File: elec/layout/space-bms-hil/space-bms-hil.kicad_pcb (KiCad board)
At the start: 4 copper layers, 90 x 70 mm, 135 parts, among them U1 10nF ±10% 50V X7R, U10 12.4kΩ ±1% 62.5mW, U100 1kΩ ±1% 62.5mW, U102 1kΩ ±1% 62.5mW, U105 10kΩ ±1% 62.5mW, U106 1kΩ ±1% 62.5mW, U108 1kΩ ±1% 62.5mW, U11 1nF ±10% 50V X7R, U12 220Ω ±1% 62.5mW, U13 1MΩ ±1% 62.5mW, U15 10pF ±5% 50V C0G, U16 10pF ±5% 50V C0G, U19 10nF ±10% 50V X7R, U2 220Ω ±1% 62.5mW, U20 6.8nF ±10% 50V X7R, U21 33Ω ±1% 62.5mW, U22 49.9Ω ±1% 62.5mW, U23 6.8nF ±10% 50V X7R, U24 33Ω ±1% 62.5mW, U25 49.9Ω ±1% 62.5mW, U26 4.7µF ±10% 10V X5R, U27 22nF ±10% 50V X7R, U28 10Ω ±1% 62.5mW, U29 33Ω ±1% 62.5mW, U3 10µF ±10% 25V X5R, U30 49.9Ω ±1% 62.5mW, U31 33Ω ±1% 62.5mW, U32 49.9Ω ±1% 62.5mW, U34 10µF ±10% 25V X5R, U35 10µF ±10% 25V X5R, U37 10kΩ ±1% 62.5mW, U39 10kΩ ±1% 62.5mW, U4 100nF ±10% 16V X7R, U41 100nF ±10% 16V X7R, U42 100nF ±10% 16V X7R, U43 2.2µF ±10% 25V X5R, U45 10kΩ ±1% 62.5mW, U46 10kΩ ±1% 62.5mW, U47 10kΩ ±1% 62.5mW, U48 10kΩ ±1% 62.5mW, U49 10kΩ ±1% 62.5mW, U5 100nF ±10% 16V X7R, U50 10kΩ ±1% 62.5mW, U51 10kΩ ±1% 62.5mW, U52 10kΩ ±1% 62.5mW, U53 10kΩ ±1% 62.5mW, U54 10kΩ ±1% 62.5mW, U55 10kΩ ±1% 62.5mW, U56 10kΩ ±1% 62.5mW, U57 10kΩ ±1% 62.5mW, U58 10kΩ ±1% 62.5mW, U59 10kΩ ±1% 62.5mW, U6 100nF ±10% 16V X7R, U60 10kΩ ±1% 62.5mW, U61 10kΩ ±1% 62.5mW, U62 10kΩ ±1% 62.5mW, U63 10kΩ ±1% 62.5mW, U66 100nF ±10% 16V X7R, U67 1kΩ ±1% 62.5mW, U68 10kΩ ±1% 62.5mW, U69 10kΩ ±1% 62.5mW, U7 100nF ±10% 16V X7R, U72 100nF ±10% 16V X7R, U73 1kΩ ±1% 62.5mW, U74 10kΩ ±1% 62.5mW, U75 10kΩ ±1% 62.5mW, U78 100nF ±10% 16V X7R, U79 1kΩ ±1% 62.5mW, U8 100nF ±10% 16V X7R, U80 10kΩ ±1% 62.5mW, U81 10kΩ ±1% 62.5mW, U84 100nF ±10% 16V X7R, U85 1kΩ ±1% 62.5mW, U86 1kΩ ±1% 62.5mW, U87 1kΩ ±1% 62.5mW, U88 1µF ±10% 25V X5R, U9 100nF ±10% 16V X7R, U90 1µF ±10% 25V X5R, U91 470nF ±20% 16V X5R, U92 1kΩ ±1% 62.5mW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

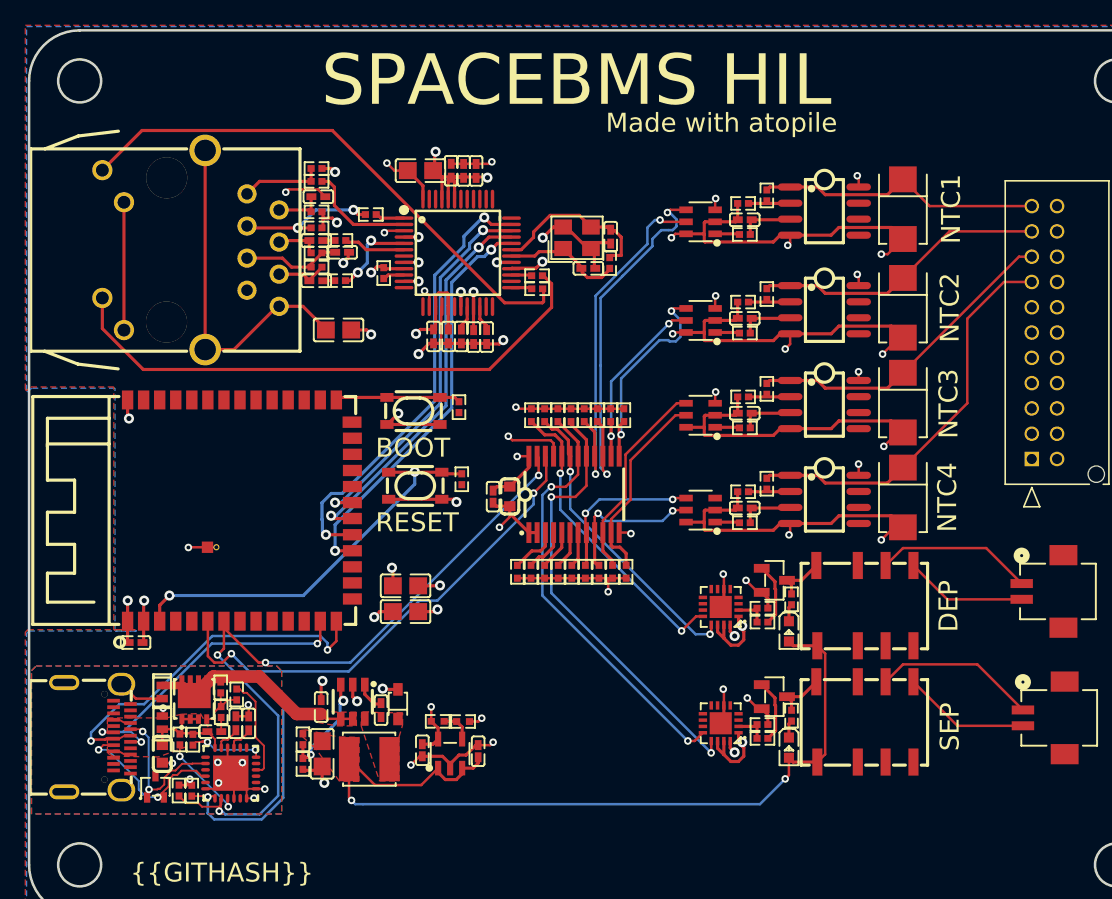
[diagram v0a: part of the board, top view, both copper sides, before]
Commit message: remove default build, build everything locally
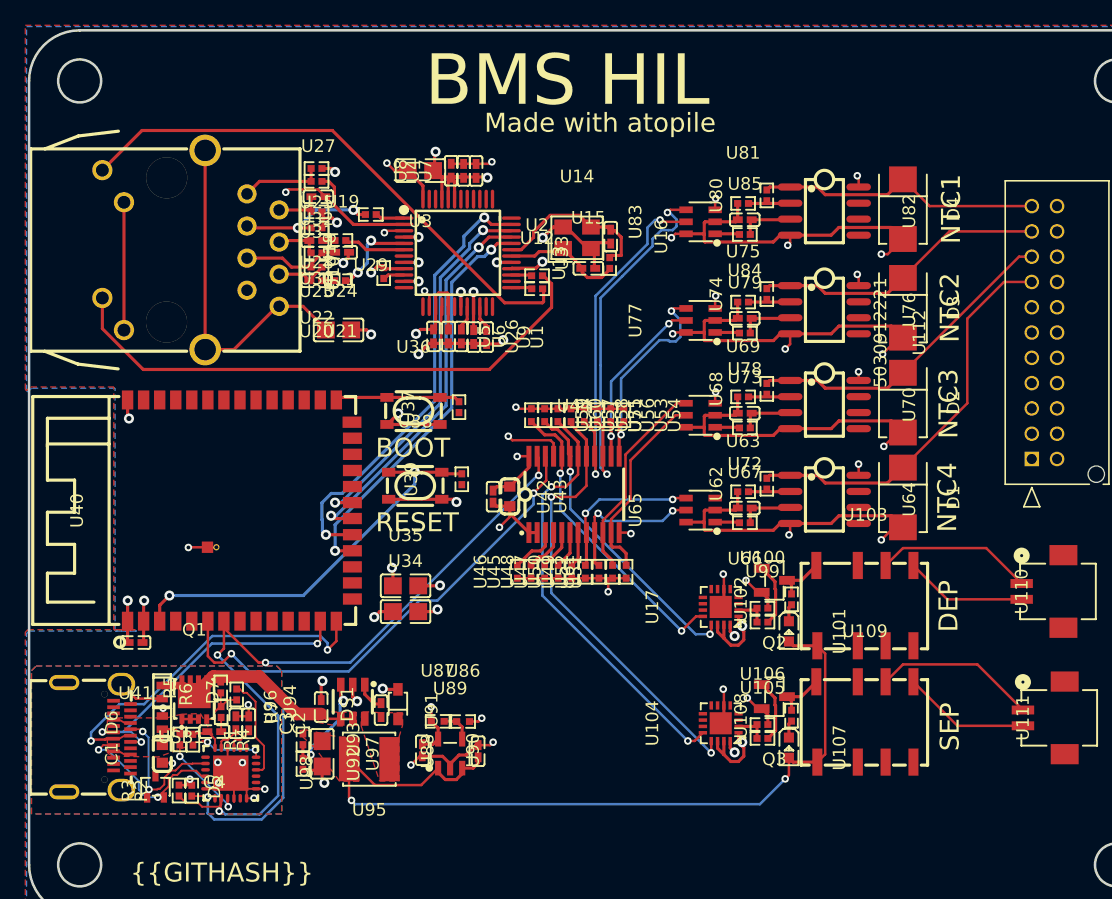
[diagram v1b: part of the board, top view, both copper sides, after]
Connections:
- net ADJ_NC renamed regulator_3v3-out
- net RESET_ renamed i2c_multiplexer-io
- net out renamed regulator_5v-out
- D1 pad 1: io-1 -> io-3
- D3 pad 1: io-2 -> io-1
- D4 pad 1: io-3 -> io-2
- DS1 pad 1: cathode-2 -> cathode-1
- R2 pad 1: line-10 -> line-9
- R3 pad 1: line-8 -> line-3
- U103 pad 5: hv-3 -> hv-1
- U104 pad 10: sep_relay.gpio_expander-net-4 -> sep_relay.gpio_expander-net-3
- U104 pad 12: line-2 -> line-10
- U104 pad 13: line-12 -> line-2
- U104 pad 3: sep_relay.gpio_expander-net-3 -> sep_relay.gpio_expander-net-1
- U104 pad 4: sep_relay.gpio_expander-net -> sep_relay.gpio_expander-net-5
- U104 pad 5: sep_relay.gpio_expander-net-5 -> sep_relay.gpio_expander-net-2
- U104 pad 7: sep_relay.gpio_expander-net-2 -> sep_relay.gpio_expander-net-4
- U104 pad 8: sep_relay.gpio_expander-net-6 -> sep_relay.gpio_expander-net
- U104 pad 9: sep_relay.gpio_expander-net-1 -> sep_relay.gpio_expander-net-6
- U107 pad 1: cathode-1 -> cathode-2
- U108 pad 1: cathode-1 -> cathode-2
- U109 pad 3: sep_relay-gnd-1 -> sep_relay-gnd
- U109 pad 4: sep_relay-gnd -> sep_relay-gnd-1
- U109 pad 6: hv-1 -> hv-3
- U110 pad 2: hv-3 -> hv-1
- U111 pad 1: hv-1 -> hv-3
- U112 pad 1: vsh_connector-net-7 -> vsh_connector-net-8
- U112 pad 10: vsh_connector-net -> vsh_connector-net-4
- U112 pad 11: vsh_connector-net-10 -> vsh_connector-net-9
- U112 pad 12: vsh_connector-net-9 -> vsh_connector-net-12
- U112 pad 13: vsh_connector-net-2 -> vsh_connector-net-10
- U112 pad 14: vsh_connector-net-1 -> vsh_connector-net
- U112 pad 15: io-1 -> io-3
- U112 pad 19: io-2 -> io-1
- U112 pad 2: vsh_connector-net-3 -> vsh_connector-net-1
- U112 pad 21: io-3 -> io-2
- U112 pad 3: vsh_connector-net-6 -> vsh_connector-net-13
- U112 pad 4: vsh_connector-net-8 -> vsh_connector-net-11
- U112 pad 5: vsh_connector-net-13 -> vsh_connector-net-6
- U112 pad 6: vsh_connector-net-11 -> vsh_connector-net-7
- U112 pad 7: vsh_connector-net-4 -> vsh_connector-net-2
- U112 pad 8: vsh_connector-net-12 -> vsh_connector-net-5
- U112 pad 9: vsh_connector-net-5 -> vsh_connector-net-3
- U17 pad 10: dep_relay.gpio_expander-net-3 -> dep_relay.gpio_expander-net-4
- U17 pad 12: line-3 -> line-5
- U17 pad 13: line-11 -> line-4
- U17 pad 3: dep_relay.gpio_expander-net-4 -> dep_relay.gpio_expander-net-1
- U17 pad 4: dep_relay.gpio_expander-net-5 -> dep_relay.gpio_expander-net-6
- U17 pad 5: dep_relay.gpio_expander-net-2 -> dep_relay.gpio_expander-net
- U17 pad 7: dep_relay.gpio_expander-net -> dep_relay.gpio_expander-net-2
- U17 pad 8: dep_relay.gpio_expander-net-6 -> dep_relay.gpio_expander-net-5
- U17 pad 9: dep_relay.gpio_expander-net-1 -> dep_relay.gpio_expander-net-3
- U40 pad 6: line-10 -> line-9
- U40 pad 7: line-8 -> line-3
- U44 pad 10: line-6 -> line-11
- U44 pad 11: line-5 -> line-7
- U44 pad 13: line-4 -> line-6
- U44 pad 14: line-9 -> line
- U44 pad 15: line-13 -> line-12
- U44 pad 16: line -> line-13
- U44 pad 17: line-12 -> line-2
- U44 pad 18: line-2 -> line-10
- U44 pad 19: line-11 -> line-4
- U44 pad 20: line-3 -> line-5
- U44 pad 22: line-10 -> line-9
- U44 pad 23: line-8 -> line-3
- U44 pad 4: i2c_multiplexer-line-3 -> i2c_multiplexer-line-2
- U44 pad 5: i2c_multiplexer-line-2 -> i2c_multiplexer-line-3
- U44 pad 9: line-7 -> line-8
- U45 pad 2: i2c_multiplexer-line-2 -> i2c_multiplexer-line-3
- U46 pad 2: i2c_multiplexer-line-3 -> i2c_multiplexer-line-2
- U49 pad 2: line-7 -> line-8
- U51 pad 2: line-5 -> line-7
- U52 pad 2: line-6 -> line-11
- U53 pad 2: line-9 -> line
- U54 pad 2: line-4 -> line-6
- U55 pad 2: line -> line-13
- U56 pad 2: line-13 -> line-12
- U57 pad 2: line-2 -> line-10
- U58 pad 2: line-12 -> line-2
- U59 pad 2: line-3 -> line-5
- U60 pad 2: line-11 -> line-4
- U62 pad 2: io-1 -> io-3
- U64 pad 1: io-1 -> io-3
- U64 pad 3: non_inverting-1 -> non_inverting
- U65 pad 5: line-7 -> line-8
- U66 pad 1: non_inverting-1 -> non_inverting
- U67 pad 2: non_inverting-1 -> non_inverting
- U70 pad 3: non_inverting -> non_inverting-1
- U71 pad 4: line-6 -> line-11
- U71 pad 5: line-5 -> line-7
- U72 pad 1: non_inverting -> non_inverting-1
- U73 pad 2: non_inverting -> non_inverting-1
- U74 pad 1: inverting -> inverting-3
- U74 pad 2: io-2 -> io-1
- U75 pad 2: inverting -> inverting-3
- U76 pad 1: io-2 -> io-1
- U76 pad 2: inverting -> inverting-3
- U76 pad 3: non_inverting-3 -> non_inverting-2
- U77 pad 4: line-4 -> line-6
- U77 pad 5: line-9 -> line
- U78 pad 1: non_inverting-3 -> non_inverting-2
- U79 pad 2: non_inverting-3 -> non_inverting-2
- U80 pad 1: inverting-3 -> inverting
- U80 pad 2: io-3 -> io-2
- U81 pad 2: inverting-3 -> inverting
- U82 pad 1: io-3 -> io-2
- U82 pad 2: inverting-3 -> inverting
- U82 pad 3: non_inverting-2 -> non_inverting-3
- U83 pad 4: line-13 -> line-12
- U83 pad 5: line -> line-13
- U84 pad 1: non_inverting-2 -> non_inverting-3
- U85 pad 2: non_inverting-2 -> non_inverting-3
- U91 pad 2: cathode-2 -> cathode-1
- U94 pad 6: cathode-2 -> cathode-1
- U95 pad 1: cathode-2 -> cathode-1
- U98 pad 1: usb_pd.pd_controller.pd_controller-line -> usb_pd.pd_controller.pd_controller-line-1
- U98 pad 5: usb_pd.pd_controller.pd_controller-line-1 -> usb_pd.pd_controller.pd_controller-line
- U98 pad 7: line-10 -> line-9
- U98 pad 8: line-8 -> line-3
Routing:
- net line-8: track 61.0 -> 12.0 mm, vias 4 -> 2
- net line-9: track 15.0 -> 60.8 mm, vias 2 -> 3
- net line-3: track 24.2 -> 61.0 mm, vias 2 -> 4
- net line-10: track 60.8 -> 34.0 mm, vias 3 -> 2
- net line: track 29.1 -> 15.0 mm
- net io-3: track 22.7 -> 31.8 mm
- net line-5: track 15.6 -> 24.2 mm, vias 0 -> 2
- net io-1: track 31.8 -> 23.3 mm
- net line-11: track 24.0 -> 16.3 mm, vias 2 -> 0
- net line-4: track 17.0 -> 24.0 mm
- net line-12: track 35.1 -> 30.3 mm
- net line-7: track 12.0 -> 15.6 mm, vias 2 -> 0
- net hv-3: track 9.67 -> 12.9 mm
- net hv-1: track 12.9 -> 9.67 mm
- net cathode-2: track 0.00 -> 1.39 mm
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- added copper zone on F.Cu, net cathode-1
- removed copper zone on F.Cu, net cathode-2
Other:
- board text added: "BMS HIL"
- board text removed: "SPACEBMS HIL"

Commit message: fix resistor values while solver isnt ready
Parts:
- U67, U73, U79, U85, U86, U92: value 1kΩ ±1% 62.5mW -> 10kΩ ±1% 62.5mW
- U87: value 1kΩ ±1% 62.5mW -> 18kΩ ±0% 62.5mW
- U93: value 1kΩ ±1% 62.5mW -> 56kΩ ±0% 62.5mW
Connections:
- net regulator_3v3-out renamed ADJ_NC
- net regulator_5v-out renamed out
- D1 pad 1: io-3 -> io-2
- D2 pad 1: io -> io-3
- D4 pad 1: io-2 -> io
- DS1 pad 1: cathode-1 -> cathode
- R2 pad 1: line-9 -> line-5
- R3 pad 1: line-3 -> line-11
- U101 pad 1: cathode -> cathode-2
- U102 pad 1: cathode -> cathode-2
- U103 pad 3: dep_relay-gnd -> dep_relay-gnd-1
- U103 pad 4: dep_relay-gnd-1 -> dep_relay-gnd
- U103 pad 6: hv-2 -> hv-4
- U104 pad 1: hv-4 -> hv-3
- U104 pad 10: sep_relay.gpio_expander-net-3 -> sep_relay.gpio_expander-net-1
- U104 pad 13: line-2 -> line-8
- U104 pad 14: hv-4 -> hv-3
- U104 pad 15: hv-4 -> hv-3
- U104 pad 3: sep_relay.gpio_expander-net-1 -> sep_relay.gpio_expander-net-3
- U104 pad 4: sep_relay.gpio_expander-net-5 -> sep_relay.gpio_expander-net-6
- U104 pad 5: sep_relay.gpio_expander-net-2 -> sep_relay.gpio_expander-net-4
- U104 pad 7: sep_relay.gpio_expander-net-4 -> sep_relay.gpio_expander-net
- U104 pad 8: sep_relay.gpio_expander-net -> sep_relay.gpio_expander-net-5
- U104 pad 9: sep_relay.gpio_expander-net-6 -> sep_relay.gpio_expander-net-2
- U107 pad 1: cathode-2 -> cathode-1
- U108 pad 1: cathode-2 -> cathode-1
- U109 pad 3: sep_relay-gnd -> sep_relay-gnd-1
- U109 pad 4: sep_relay-gnd-1 -> sep_relay-gnd
- U109 pad 6: hv-3 -> hv-2
- U110 pad 1: hv-2 -> hv-4
- U111 pad 1: hv-3 -> hv-2
- U112 pad 1: vsh_connector-net-8 -> vsh_connector-net-2
- U112 pad 10: vsh_connector-net-4 -> vsh_connector-net-3
- U112 pad 11: vsh_connector-net-9 -> vsh_connector-net-7
- U112 pad 13: vsh_connector-net-10 -> vsh_connector-net-11
- U112 pad 14: vsh_connector-net -> vsh_connector-net-1
- U112 pad 15: io-3 -> io-2
- U112 pad 17: io -> io-3
- U112 pad 2: vsh_connector-net-1 -> vsh_connector-net-8
- U112 pad 21: io-2 -> io
- U112 pad 3: vsh_connector-net-13 -> vsh_connector-net-10
- U112 pad 4: vsh_connector-net-11 -> vsh_connector-net-4
- U112 pad 5: vsh_connector-net-6 -> vsh_connector-net-5
- U112 pad 6: vsh_connector-net-7 -> vsh_connector-net-13
- U112 pad 7: vsh_connector-net-2 -> vsh_connector-net-9
- U112 pad 8: vsh_connector-net-5 -> vsh_connector-net-6
- U112 pad 9: vsh_connector-net-3 -> vsh_connector-net
- U17 pad 1: hv-4 -> hv-3
- U17 pad 12: line-5 -> line-9
- U17 pad 13: line-4 -> line-6
- U17 pad 14: hv-4 -> hv-3
- U17 pad 15: hv-4 -> hv-3
- U17 pad 3: dep_relay.gpio_expander-net-1 -> dep_relay.gpio_expander-net-2
- U17 pad 4: dep_relay.gpio_expander-net-6 -> dep_relay.gpio_expander-net
- U17 pad 5: dep_relay.gpio_expander-net -> dep_relay.gpio_expander-net-6
- U17 pad 7: dep_relay.gpio_expander-net-2 -> dep_relay.gpio_expander-net-1
- U17 pad 8: dep_relay.gpio_expander-net-5 -> dep_relay.gpio_expander-net-3
- U17 pad 9: dep_relay.gpio_expander-net-3 -> dep_relay.gpio_expander-net-5
- U18 pad 10: hv-4 -> hv-3
- U18 pad 12: hv-4 -> hv-3
- U20 pad 1: controller.ethernet-net-1 -> controller.ethernet-net
- U21 pad 2: controller.ethernet-net-1 -> controller.ethernet-net
- U23 pad 1: controller.ethernet-net -> controller.ethernet-net-1
- U24 pad 2: controller.ethernet-net -> controller.ethernet-net-1
- U28 pad 1: hv-4 -> hv-3
- U3 pad 1: hv-4 -> hv-3
- U30 pad 1: hv-4 -> hv-3
- U32 pad 1: hv-4 -> hv-3
- U33 pad 11: hv-4 -> hv-3
- U33 pad 15: hv-4 -> hv-3
- U33 pad 17: hv-4 -> hv-3
- U33 pad 21: hv-4 -> hv-3
- U33 pad 28: hv-4 -> hv-3
- U33 pad 4: hv-4 -> hv-3
- U33 pad 43: hv-4 -> hv-3
- U33 pad 44: hv-4 -> hv-3
- U33 pad 45: hv-4 -> hv-3
- U33 pad 8: hv-4 -> hv-3
- U34 pad 1: hv-4 -> hv-3
- U35 pad 1: hv-4 -> hv-3
- U36 pad 1: in -> in-1
- U36 pad 2: in -> in-1
- U37 pad 1: hv-4 -> hv-3
- U37 pad 2: in -> in-1
- U38 pad 1: in-1 -> in
- U38 pad 2: in-1 -> in
- U39 pad 1: hv-4 -> hv-3
- U39 pad 2: in-1 -> in
- U4 pad 1: hv-4 -> hv-3
- U40 pad 2: hv-4 -> hv-3
- U40 pad 27: in -> in-1
- U40 pad 3: in-1 -> in
- U40 pad 6: line-9 -> line-5
- U40 pad 7: line-3 -> line-11
- U41 pad 1: hv-4 -> hv-3
- U42 pad 1: hv-4 -> hv-3
- U43 pad 1: hv-4 -> hv-3
- U44 pad 10: line-11 -> line-12
- U44 pad 11: line-7 -> line-13
- U44 pad 13: line-6 -> line-3
- U44 pad 14: line -> line-1
- U44 pad 15: line-12 -> line-4
- U44 pad 16: line-13 -> line
- U44 pad 17: line-2 -> line-8
- U44 pad 19: line-4 -> line-6
- U44 pad 20: line-5 -> line-9
- U44 pad 22: line-9 -> line-5
- U44 pad 23: line-3 -> line-11
- U44 pad 24: hv-4 -> hv-3
- U44 pad 4: i2c_multiplexer-line-2 -> i2c_multiplexer-line
- U44 pad 7: i2c_multiplexer-line -> i2c_multiplexer-line-2
- U44 pad 8: line-1 -> line-2
- U44 pad 9: line-8 -> line-7
- U45 pad 1: hv-4 -> hv-3
- U46 pad 1: hv-4 -> hv-3
- U46 pad 2: i2c_multiplexer-line-2 -> i2c_multiplexer-line
- U47 pad 1: hv-4 -> hv-3
- U47 pad 2: i2c_multiplexer-line -> i2c_multiplexer-line-2
- U48 pad 1: hv-4 -> hv-3
- U49 pad 1: hv-4 -> hv-3
- U49 pad 2: line-8 -> line-7
- U5 pad 1: hv-4 -> hv-3
- U50 pad 1: hv-4 -> hv-3
- U50 pad 2: line-1 -> line-2
- U51 pad 1: hv-4 -> hv-3
- U51 pad 2: line-7 -> line-13
- U52 pad 1: hv-4 -> hv-3
- U52 pad 2: line-11 -> line-12
- U53 pad 1: hv-4 -> hv-3
- U53 pad 2: line -> line-1
- U54 pad 1: hv-4 -> hv-3
- U54 pad 2: line-6 -> line-3
- U55 pad 1: hv-4 -> hv-3
- U55 pad 2: line-13 -> line
- U56 pad 1: hv-4 -> hv-3
- U56 pad 2: line-12 -> line-4
- U57 pad 1: hv-4 -> hv-3
- U58 pad 1: hv-4 -> hv-3
- U58 pad 2: line-2 -> line-8
- U59 pad 1: hv-4 -> hv-3
- U59 pad 2: line-5 -> line-9
- U6 pad 1: hv-4 -> hv-3
- U60 pad 1: hv-4 -> hv-3
- U60 pad 2: line-4 -> line-6
- U61 pad 2: hv-4 -> hv-3
- U62 pad 1: inverting-2 -> inverting-3
- U62 pad 2: io-3 -> io-2
- U63 pad 2: inverting-2 -> inverting-3
- U64 pad 1: io-3 -> io-2
- U64 pad 2: inverting-2 -> inverting-3
- U64 pad 3: non_inverting -> non_inverting-2
- U64 pad 8: hv-4 -> hv-3
- U65 pad 3: hv-4 -> hv-3
- U65 pad 4: line-1 -> line-2
- U65 pad 5: line-8 -> line-7
- U66 pad 1: non_inverting -> non_inverting-2
- U67 pad 2: non_inverting -> non_inverting-2
- U68 pad 1: inverting-1 -> inverting-2
- U68 pad 2: io -> io-3
- U69 pad 2: inverting-1 -> inverting-2
- U7 pad 1: hv-4 -> hv-3
- U70 pad 1: io -> io-3
- U70 pad 2: inverting-1 -> inverting-2
- U70 pad 8: hv-4 -> hv-3
- U71 pad 3: hv-4 -> hv-3
- U71 pad 4: line-11 -> line-12
- U71 pad 5: line-7 -> line-13
- U74 pad 1: inverting-3 -> inverting
- U75 pad 2: inverting-3 -> inverting
- U76 pad 2: inverting-3 -> inverting
- U76 pad 3: non_inverting-2 -> non_inverting
- U76 pad 8: hv-4 -> hv-3
- U77 pad 3: hv-4 -> hv-3
- U77 pad 4: line-6 -> line-3
- U77 pad 5: line -> line-1
- U78 pad 1: non_inverting-2 -> non_inverting
- U79 pad 2: non_inverting-2 -> non_inverting
- U8 pad 1: hv-4 -> hv-3
- U80 pad 1: inverting -> inverting-1
- U80 pad 2: io-2 -> io
- U81 pad 2: inverting -> inverting-1
- U82 pad 1: io-2 -> io
- U82 pad 2: inverting -> inverting-1
- U82 pad 8: hv-4 -> hv-3
- U83 pad 3: hv-4 -> hv-3
- U83 pad 4: line-12 -> line-4
- U83 pad 5: line-13 -> line
- U87 pad 1: hv-4 -> hv-3
- U89 pad 5: hv-4 -> hv-3
- U9 pad 1: hv-4 -> hv-3
- U90 pad 1: hv-4 -> hv-3
- U91 pad 2: cathode-1 -> cathode
- U94 pad 6: cathode-1 -> cathode
- U95 pad 1: cathode-1 -> cathode
- U98 pad 7: line-9 -> line-5
- U98 pad 8: line-3 -> line-11
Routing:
- net hv-4: track 98.6 -> 12.5 mm, vias 26 -> 0
- net hv-3: track 12.9 -> 98.6 mm, vias 0 -> 26
- net line-11: track 16.3 -> 61.0 mm, vias 0 -> 4
- net line-3: track 61.0 -> 17.0 mm, vias 4 -> 2
- net line-9: track 60.8 -> 24.2 mm, vias 3 -> 2
- net line-5: track 24.2 -> 60.8 mm, vias 2 -> 3
- net line-8: track 12.0 -> 35.1 mm
- net line-2: track 35.1 -> 12.7 mm
- net in-1: track 32.2 -> 9.92 mm, vias 2 -> 0
- net in: track 9.92 -> 32.2 mm, vias 0 -> 2
- net line: track 15.0 -> 29.1 mm
- net line-12: track 30.3 -> 16.3 mm, vias 2 -> 0
- net line-13: track 29.1 -> 15.6 mm, vias 2 -> 0
- net io-2: track 22.7 -> 31.8 mm
- net line-6: track 17.0 -> 24.0 mm
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- added copper zone on F.Cu, net cathode
- added copper zone on F.Cu, net hv-3
- added copper zone on In2.Cu, net hv-3
- removed copper zone on F.Cu, net cathode-1
- removed copper zone on F.Cu, net hv-4
- removed copper zone on In2.Cu, net hv-4

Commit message: add module builds back in to ato.yaml with mfg-data excluded in config
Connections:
- net A2 renamed SSTXP1
- net A3 renamed SSTXN1
- net A8 renamed SBU1
- net ADJ_NC renamed regulator_3v3-out
- net B10 renamed SSRXN1
- net B11 renamed SSRXP1
- net SBU2 renamed B8
- net SSRXN2 renamed A10
- net SSRXP2 renamed A11
- net SSTXN2 renamed B3
- net SSTXP2 renamed B2
- net out renamed regulator_5v-out
- D1 pad 1: io-2 -> io-3
- D2 pad 1: io-3 -> io-2
- DS1 pad 1: cathode -> cathode-1
- R2 pad 1: line-5 -> line-13
- R3 pad 1: line-11 -> line-3
- U103 pad 3: dep_relay-gnd-1 -> dep_relay-gnd
- U103 pad 4: dep_relay-gnd -> dep_relay-gnd-1
- U103 pad 5: hv-1 -> hv-3
- U104 pad 1: hv-3 -> hv-2
- U104 pad 10: sep_relay.gpio_expander-net-1 -> sep_relay.gpio_expander-net-3
- U104 pad 12: line-10 -> line-2
- U104 pad 13: line-8 -> line-5
- U104 pad 14: hv-3 -> hv-2
- U104 pad 15: hv-3 -> hv-2
- U104 pad 3: sep_relay.gpio_expander-net-3 -> sep_relay.gpio_expander-net
- U104 pad 4: sep_relay.gpio_expander-net-6 -> sep_relay.gpio_expander-net-1
- U104 pad 5: sep_relay.gpio_expander-net-4 -> sep_relay.gpio_expander-net-2
- U104 pad 7: sep_relay.gpio_expander-net -> sep_relay.gpio_expander-net-4
- U104 pad 8: sep_relay.gpio_expander-net-5 -> sep_relay.gpio_expander-net-6
- U104 pad 9: sep_relay.gpio_expander-net-2 -> sep_relay.gpio_expander-net-5
- U107 pad 1: cathode-1 -> cathode
- U108 pad 1: cathode-1 -> cathode
- U109 pad 5: hv -> hv-1
- U109 pad 6: hv-2 -> hv
- U110 pad 2: hv-1 -> hv-3
- U111 pad 1: hv-2 -> hv
- U111 pad 2: hv -> hv-1
- U112 pad 1: vsh_connector-net-2 -> vsh_connector-net-10
- U112 pad 11: vsh_connector-net-7 -> vsh_connector-net-12
- U112 pad 12: vsh_connector-net-12 -> vsh_connector-net-9
- U112 pad 13: vsh_connector-net-11 -> vsh_connector-net-6
- U112 pad 14: vsh_connector-net-1 -> vsh_connector-net-5
- U112 pad 15: io-2 -> io-3
- U112 pad 17: io-3 -> io-2
- U112 pad 2: vsh_connector-net-8 -> vsh_connector-net-1
- U112 pad 3: vsh_connector-net-10 -> vsh_connector-net
- U112 pad 5: vsh_connector-net-5 -> vsh_connector-net-7
- U112 pad 6: vsh_connector-net-13 -> vsh_connector-net-11
- U112 pad 7: vsh_connector-net-9 -> vsh_connector-net-8
- U112 pad 8: vsh_connector-net-6 -> vsh_connector-net-2
- U112 pad 9: vsh_connector-net -> vsh_connector-net-13
- U17 pad 1: hv-3 -> hv-2
- U17 pad 10: dep_relay.gpio_expander-net-4 -> dep_relay.gpio_expander-net-2
- U17 pad 12: line-9 -> line-8
- U17 pad 13: line-6 -> line-9
- U17 pad 14: hv-3 -> hv-2
- U17 pad 15: hv-3 -> hv-2
- U17 pad 3: dep_relay.gpio_expander-net-2 -> dep_relay.gpio_expander-net-1
- U17 pad 5: dep_relay.gpio_expander-net-6 -> dep_relay.gpio_expander-net-4
- U17 pad 7: dep_relay.gpio_expander-net-1 -> dep_relay.gpio_expander-net-3
- U17 pad 8: dep_relay.gpio_expander-net-3 -> dep_relay.gpio_expander-net-6
- U18 pad 10: hv-3 -> hv-2
- U18 pad 12: hv-3 -> hv-2
- U20 pad 1: controller.ethernet-net -> controller.ethernet-net-1
- U21 pad 2: controller.ethernet-net -> controller.ethernet-net-1
- U23 pad 1: controller.ethernet-net-1 -> controller.ethernet-net
- U24 pad 2: controller.ethernet-net-1 -> controller.ethernet-net
- U28 pad 1: hv-3 -> hv-2
- U3 pad 1: hv-3 -> hv-2
- U30 pad 1: hv-3 -> hv-2
- U32 pad 1: hv-3 -> hv-2
- U33 pad 11: hv-3 -> hv-2
- U33 pad 15: hv-3 -> hv-2
- U33 pad 17: hv-3 -> hv-2
- U33 pad 21: hv-3 -> hv-2
- U33 pad 28: hv-3 -> hv-2
- U33 pad 4: hv-3 -> hv-2
- U33 pad 43: hv-3 -> hv-2
- U33 pad 44: hv-3 -> hv-2
- U33 pad 45: hv-3 -> hv-2
- U33 pad 8: hv-3 -> hv-2
- U34 pad 1: hv-3 -> hv-2
- U35 pad 1: hv-3 -> hv-2
- U37 pad 1: hv-3 -> hv-2
- U39 pad 1: hv-3 -> hv-2
- U4 pad 1: hv-3 -> hv-2
- U40 pad 2: hv-3 -> hv-2
- U40 pad 6: line-5 -> line-13
- U40 pad 7: line-11 -> line-3
- U41 pad 1: hv-3 -> hv-2
- U42 pad 1: hv-3 -> hv-2
- U43 pad 1: hv-3 -> hv-2
- U44 pad 10: line-12 -> line-11
- U44 pad 11: line-13 -> line-12
- U44 pad 13: line-3 -> line
- U44 pad 14: line-1 -> line-7
- U44 pad 15: line-4 -> line-1
- U44 pad 16: line -> line-10
- U44 pad 17: line-8 -> line-5
- U44 pad 18: line-10 -> line-2
- U44 pad 19: line-6 -> line-9
- U44 pad 20: line-9 -> line-8
- U44 pad 22: line-5 -> line-13
- U44 pad 23: line-11 -> line-3
- U44 pad 24: hv-3 -> hv-2
- U44 pad 4: i2c_multiplexer-line -> i2c_multiplexer-line-1
- U44 pad 5: i2c_multiplexer-line-3 -> i2c_multiplexer-line
- U44 pad 6: i2c_multiplexer-line-1 -> i2c_multiplexer-line-2
- U44 pad 7: i2c_multiplexer-line-2 -> i2c_multiplexer-line-3
- U44 pad 8: line-2 -> line-6
- U44 pad 9: line-7 -> line-4
- U45 pad 1: hv-3 -> hv-2
- U45 pad 2: i2c_multiplexer-line-3 -> i2c_multiplexer-line
- U46 pad 1: hv-3 -> hv-2
- U46 pad 2: i2c_multiplexer-line -> i2c_multiplexer-line-1
- U47 pad 1: hv-3 -> hv-2
- U47 pad 2: i2c_multiplexer-line-2 -> i2c_multiplexer-line-3
- U48 pad 1: hv-3 -> hv-2
- U48 pad 2: i2c_multiplexer-line-1 -> i2c_multiplexer-line-2
- U49 pad 1: hv-3 -> hv-2
- U49 pad 2: line-7 -> line-4
- U5 pad 1: hv-3 -> hv-2
- U50 pad 1: hv-3 -> hv-2
- U50 pad 2: line-2 -> line-6
- U51 pad 1: hv-3 -> hv-2
- U51 pad 2: line-13 -> line-12
- U52 pad 1: hv-3 -> hv-2
- U52 pad 2: line-12 -> line-11
- U53 pad 1: hv-3 -> hv-2
- U53 pad 2: line-1 -> line-7
- U54 pad 1: hv-3 -> hv-2
- U54 pad 2: line-3 -> line
- U55 pad 1: hv-3 -> hv-2
- U55 pad 2: line -> line-10
- U56 pad 1: hv-3 -> hv-2
- U56 pad 2: line-4 -> line-1
- U57 pad 1: hv-3 -> hv-2
- U57 pad 2: line-10 -> line-2
- U58 pad 1: hv-3 -> hv-2
- U58 pad 2: line-8 -> line-5
- U59 pad 1: hv-3 -> hv-2
- U59 pad 2: line-9 -> line-8
- U6 pad 1: hv-3 -> hv-2
- U60 pad 1: hv-3 -> hv-2
- U60 pad 2: line-6 -> line-9
- U61 pad 2: hv-3 -> hv-2
- U62 pad 2: io-2 -> io-3
- U64 pad 1: io-2 -> io-3
- U64 pad 3: non_inverting-2 -> non_inverting
- U64 pad 8: hv-3 -> hv-2
- U65 pad 3: hv-3 -> hv-2
- U65 pad 4: line-2 -> line-6
- U65 pad 5: line-7 -> line-4
- U66 pad 1: non_inverting-2 -> non_inverting
- U67 pad 2: non_inverting-2 -> non_inverting
- U68 pad 1: inverting-2 -> inverting-1
- U68 pad 2: io-3 -> io-2
- U69 pad 2: inverting-2 -> inverting-1
- U7 pad 1: hv-3 -> hv-2
- U70 pad 1: io-3 -> io-2
- U70 pad 2: inverting-2 -> inverting-1
- U70 pad 3: non_inverting-1 -> non_inverting-2
- U70 pad 8: hv-3 -> hv-2
- U71 pad 3: hv-3 -> hv-2
- U71 pad 4: line-12 -> line-11
- U71 pad 5: line-13 -> line-12
- U72 pad 1: non_inverting-1 -> non_inverting-2
- U73 pad 2: non_inverting-1 -> non_inverting-2
- U76 pad 3: non_inverting -> non_inverting-1
- U76 pad 8: hv-3 -> hv-2
- U77 pad 3: hv-3 -> hv-2
- U77 pad 4: line-3 -> line
- U77 pad 5: line-1 -> line-7
- U78 pad 1: non_inverting -> non_inverting-1
- U79 pad 2: non_inverting -> non_inverting-1
- U8 pad 1: hv-3 -> hv-2
- U80 pad 1: inverting-1 -> inverting-2
- U81 pad 2: inverting-1 -> inverting-2
- U82 pad 2: inverting-1 -> inverting-2
- U82 pad 8: hv-3 -> hv-2
- U83 pad 3: hv-3 -> hv-2
- U83 pad 4: line-4 -> line-1
- U83 pad 5: line -> line-10
- U87 pad 1: hv-3 -> hv-2
- U89 pad 5: hv-3 -> hv-2
- U9 pad 1: hv-3 -> hv-2
- U90 pad 1: hv-3 -> hv-2
- U91 pad 2: cathode -> cathode-1
- U94 pad 6: cathode -> cathode-1
- U95 pad 1: cathode -> cathode-1
- U98 pad 1: usb_pd.pd_controller.pd_controller-line-1 -> usb_pd.pd_controller.pd_controller-line
- U98 pad 5: usb_pd.pd_controller.pd_controller-line -> usb_pd.pd_controller.pd_controller-line-1
- U98 pad 7: line-5 -> line-13
- U98 pad 8: line-11 -> line-3
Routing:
- net hv-3: track 98.6 -> 9.67 mm, vias 26 -> 0
- net hv-2: track 12.9 -> 98.6 mm, vias 0 -> 26
- net line-13: track 15.6 -> 60.8 mm, vias 0 -> 3
- net line-11: track 61.0 -> 16.3 mm, vias 4 -> 0
- net line-3: track 17.0 -> 61.0 mm, vias 2 -> 4
- net line-5: track 60.8 -> 35.1 mm, vias 3 -> 2
- net line-2: track 12.7 -> 34.0 mm
- net line-4: track 30.3 -> 12.0 mm
- net line-1: track 15.0 -> 30.3 mm
- net line: track 29.1 -> 17.0 mm
- net line-6: track 24.0 -> 12.7 mm
- net line-8: track 35.1 -> 24.2 mm
- net io-3: track 25.6 -> 31.8 mm
- net io-2: track 31.8 -> 25.6 mm
- net line-10: track 34.0 -> 29.1 mm
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- added copper zone on F.Cu, net cathode-1
- added copper zone on F.Cu, net hv-2
- added copper zone on In2.Cu, net hv-2
- removed copper zone on F.Cu, net cathode
- removed copper zone on F.Cu, net hv-3
- removed copper zone on In2.Cu, net hv-3
